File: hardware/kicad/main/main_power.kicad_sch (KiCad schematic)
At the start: 20 parts, among them J1 LINK, U1 RT9080-33GJ5, U2 TPS22917DBVR

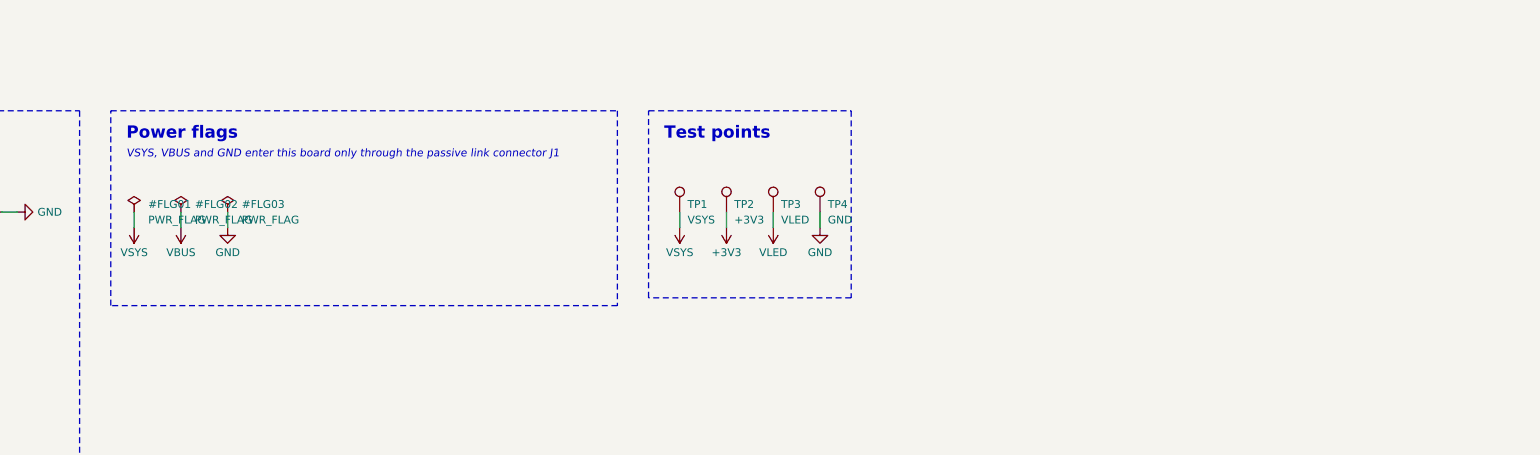
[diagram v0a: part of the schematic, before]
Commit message: Plated GND spindle holes as ESD bleed for the flywheel ring; LED B-variant caveat
Co-Authored-By: Claude Opus 5.5 <noreply@anthropic.com>
Claude-Session: https://claude.ai/code/session_01P3cqdBhxLcWY3sGUVf9LAJ
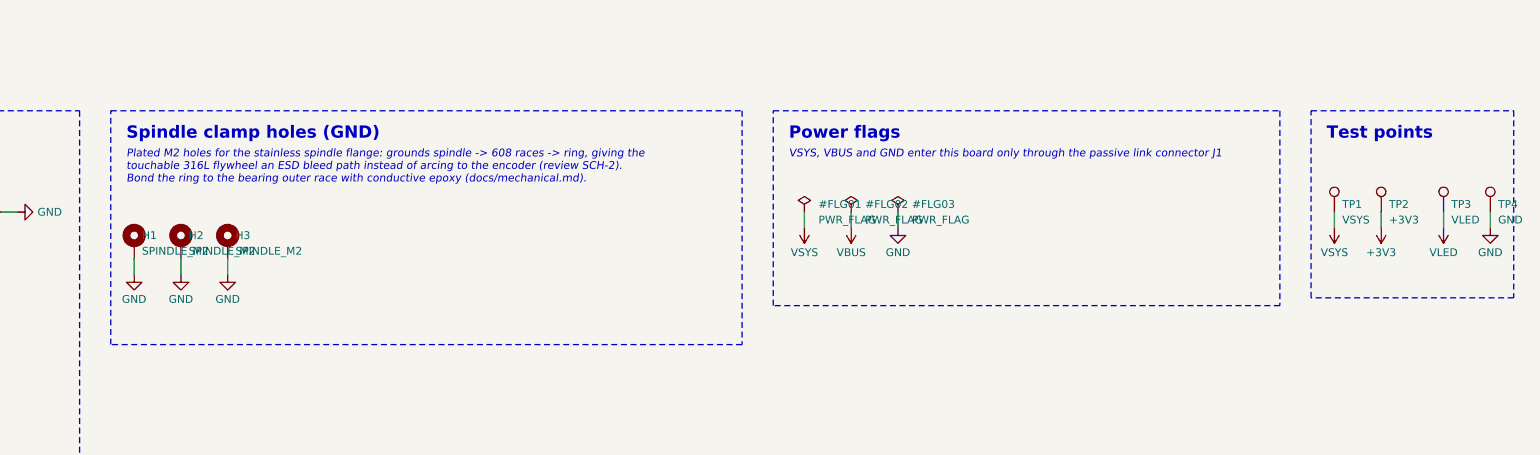
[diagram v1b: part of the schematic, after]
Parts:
- added H1, H2, H3: SPINDLE_M2, MountingHole:MountingHole_2.2mm_M2_Pad_Via, symbol Mechanical:MountingHole_Pad
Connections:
- net GND: now also H1.1, H2.1, H3.1
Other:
- note added: "Plated M2 holes for the stainless spindle flange: grounds spindle -> 608 races -> ring, giving the touchable 316L flywheel an ESD bleed path instead of arcing to the encoder (review SCH-2). Bond the ring to the bearing outer race with conductive epoxy (docs/mechanical.md)."
- note added: "Spindle clamp holes (GND)"
- moved on the sheet: TP1, TP2, TP3, TP4

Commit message: WIP: re-placed boards with fiducials (routing in progress), --finish clean-up step
Co-Authored-By: Claude Opus 5.5 <noreply@anthropic.com>
Claude-Session: https://claude.ai/code/session_01P3cqdBhxLcWY3sGUVf9LAJ
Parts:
- C1, C2, C3, C4, C5, C6, C8, C9: Manufacturer (none) -> Samsung Electro-Mechanics
- C7: Manufacturer (none) -> FH
- R1, R2, R3, R4: Manufacturer (none) -> UNI-ROYAL
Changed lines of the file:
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@@
 			)
 		)
+		(property "Manufacturer" "Samsung Electro-Mechanics"
+			(at 55.88 38.1 0)
+			(effects
+				(font
+					(size 1.27 1.27)
+				)
+				(hide yes)
+			)
+		)
 		(property "LCSC" "C45783"
 			(at 55.88 38.1 0)
@@
 			)
 		)
+		(property "Manufacturer" "Samsung Electro-Mechanics"
+			(at 193.04 35.56 0)
+			(effects
+				(font
+					(size 1.27 1.27)
+				)
+				(hide yes)
+			)
+		)
 		(property "LCSC" "C19702"
 			(at 193.04 35.56 0)
@@
 			)
 		)
+		(property "Manufacturer" "Samsung Electro-Mechanics"
+			(at 223.52 35.56 0)
+			(effects
+				(font
+					(size 1.27 1.27)
+				)
+				(hide yes)
+			)
+		)
 		(property "LCSC" "C19702"
 			(at 223.52 35.56 0)
@@
 			)
 		)
+		(property "Manufacturer" "Samsung Electro-Mechanics"
+			(at 256.54 35.56 0)
+			(effects
+				(font
+					(size 1.27 1.27)
+				)
+				(hide yes)
+			)
+		)
 		(property "LCSC" "C1525"
 			(at 256.54 35.56 0)
@@
 			)
 		)
+		(property "Manufacturer" "UNI-ROYAL"
+			(at 292.1 35.56 0)
+			(effects
+				(font
+					(size 1.27 1.27)
+				)
+				(hide yes)
+			)
+		)
 		(property "LCSC" "C11490"
 			(at 292.1 35.56 0)
@@
 			)
 		)
+		(property "Manufacturer" "UNI-ROYAL"
+			(at 337.82 35.56 0)
+			(effects
+				(font
+					(size 1.27 1.27)
+				)
+				(hide yes)
+			)
+		)
 		(property "LCSC" "C26083"
 			(at 337.82 35.56 0)
@@
 			)
 		)
+		(property "Manufacturer" "Samsung Electro-Mechanics"
+			(at 375.92 35.56 0)
+			(effects
+				(font
+					(size 1.27 1.27)
+				)
+				(hide yes)
+			)
+		)
 		(property "LCSC" "C1525"
 			(at 375.92 35.56 0)
@@
 			)
 		)
+		(property "Manufacturer" "Samsung Electro-Mechanics"
+			(at 83.82 111.76 0)
+			(effects
+				(font
+					(size 1.27 1.27)
+				)
+				(hide yes)
+			)
+		)
 		(property "LCSC" "C19702"
 			(at 83.82 111.76 0)
@@
 			)
 		)
+		(property "Manufacturer" "FH"
+			(at 116.84 111.76 0)
+			(effects
+				(font
+					(size 1.27 1.27)
+				)
+				(hide yes)
+			)
+		)
 		(property "LCSC" "C1523"
 			(at 116.84 111.76 0)
@@
 			)
 		)
+		(property "Manufacturer" "UNI-ROYAL"
+			(at 154.94 111.76 0)
+			(effects
+				(font
+					(size 1.27 1.27)
+				)
+				(hide yes)
+			)
+		)
 		(property "LCSC" "C25741"
 			(at 154.94 111.76 0)
@@
 			)
 		)
+		(property "Manufacturer" "UNI-ROYAL"
+			(at 27.94 149.86 0)
+			(effects
+				(font
+					(size 1.27 1.27)
+				)
+				(hide yes)
+			)
+		)
 		(property "LCSC" "C25076"
 			(at 27.94 149.86 0)
@@
 			)
 		)
+		(property "Manufacturer" "Samsung Electro-Mechanics"
+			(at 63.5 149.86 0)
+			(effects
+				(font
+					(size 1.27 1.27)
+				)
+				(hide yes)
+			)
+		)
 		(property "LCSC" "C45783"
 			(at 63.5 149.86 0)
@@
 			(at 96.52 149.86 0)
 			(effects
+				(font
+					(size 1.27 1.27)
+				)
+				(hide yes)
+			)
+		)
+		(property "Manufacturer" "Samsung Electro-Mechanics"
+			(at 96.52 149.86 0)
+			(effects

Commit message: Main schematic: ERC clean (VBUS_NRF power flag, documented waiver for U21 QOD tied to VOUT); Freerouting pass cap; load-switch test numerics fallback
- build.py: ERC_WAIVERS lists intended pin-type violations; waived ones are reported as such, never dropped
- mcu.py: PWR_FLAG on VBUS_NRF (fed from VBUS through R12)
- display.py: L20 note gives Isat 0.72 A rated (0.92 A typical)
- layout.py: also pass --router.max_passes (Freerouting 2.1 ignores -mp)
- test_load_switches.py: run() retries stalled/hung decks with looser numerics (verifier NEW-6)

Co-Authored-By: Claude Opus 5.5 <noreply@anthropic.com>
Claude-Session: https://claude.ai/code/session_01P3cqdBhxLcWY3sGUVf9LAJ
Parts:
- C2, C6: value 10u -> 10u/25V; LCSC C19702 -> C96446; MPN CL10A106KP8NNNC -> CL10A106MA8NRNC
- R4: value 100 -> 68; LCSC C25076 -> C163455; MPN 0402WGF1000TCE -> RC0402FR-0768RL; Manufacturer UNI-ROYAL -> YAGEO
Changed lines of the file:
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@@
 			)
 		)
-		(property "Value" "10u"
+		(property "Value" "10u/25V"
 			(at 193.04 39.192 90)
 			(effects
@@
 			)
 		)
-		(property "MPN" "CL10A106KP8NNNC"
+		(property "MPN" "CL10A106MA8NRNC"
 			(at 193.04 35.56 0)
 			(effects
@@
 			)
 		)
-		(property "LCSC" "C19702"
+		(property "LCSC" "C96446"
 			(at 193.04 35.56 0)
 			(effects
@@
 			)
 		)
-		(property "Value" "10u"
+		(property "Value" "10u/25V"
 			(at 83.82 115.392 90)
 			(effects
@@
 			)
 		)
-		(property "MPN" "CL10A106KP8NNNC"
+		(property "MPN" "CL10A106MA8NRNC"
 			(at 83.82 111.76 0)
 			(effects
@@
 			)
 		)
-		(property "LCSC" "C19702"
+		(property "LCSC" "C96446"
 			(at 83.82 111.76 0)
 			(effects
@@
 			)
 		)
-		(property "Value" "100"
+		(property "Value" "68"
 			(at 27.94 152.476 90)
 			(effects
@@
 			)
 		)
-		(property "Description" "QOD discharge resistor (TPS22917 option 1: external R between VOUT and QOD); ~4 ms with 44 uF"
+		(property "Description" "QOD discharge resistor (TPS22917 option 1: external R between VOUT and QOD); VLED to 10 % in <= 28.3 ms at the C8/C9 +20 % corner, inside the firmware's 30 ms (hardware/sim test_load_switches)"
 			(at 27.94 149.86 0)
 			(effects
@@
 			)
 		)
-		(property "MPN" "0402WGF1000TCE"
+		(property "MPN" "RC0402FR-0768RL"
 			(at 27.94 149.86 0)
 			(effects
@@
 			)
 		)
-		(property "Manufacturer" "UNI-ROYAL"
+		(property "Manufacturer" "YAGEO"
 			(at 27.94 149.86 0)
 			(effects
@@
 			)
 		)
-		(property "LCSC" "C25076"
+		(property "LCSC" "C163455"
 			(at 27.94 149.86 0)
 			(effects

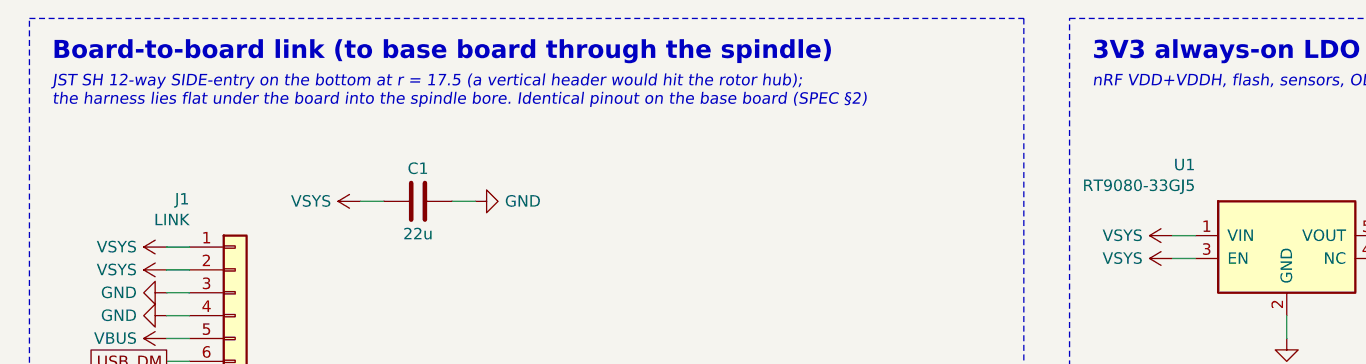
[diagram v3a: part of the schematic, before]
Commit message: Schematic notes: J1 at r 19.5, VLED fall 24/26.6 ms, hot-plug 4.49-5.49 V, SM04B J2, 100k press pull-down, SYS_REG 4.4 V, side-entry J3, LED data path and margins
Notes only; netlists unchanged. Base board still DRC-clean with schematic parity.

Co-Authored-By: Claude Opus 5.5 <noreply@anthropic.com>
Claude-Session: https://claude.ai/code/session_01P3cqdBhxLcWY3sGUVf9LAJ
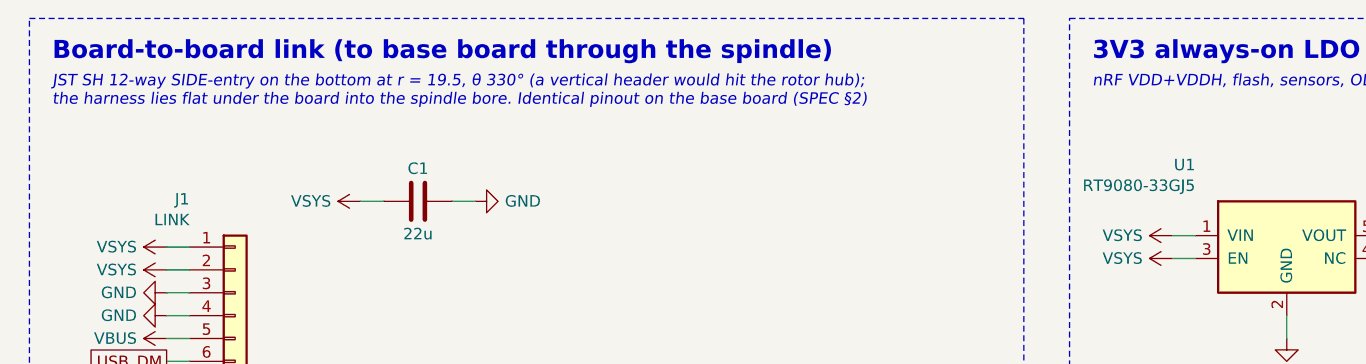
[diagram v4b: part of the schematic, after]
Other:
- note added: "JST SH 12-way SIDE-entry on the bottom at r = 19.5, θ 330° (a vertical header would hit the rotor hub); the harness lies flat under the board into the spindle bore. Identical pinout on the base board (SPEC §2)"
- note removed: "JST SH 12-way SIDE-entry on the bottom at r = 17.5 (a vertical header would hit the rotor hub); the harness lies flat under the board into the spindle bore. Identical pinout on the base board (SPEC §2)"
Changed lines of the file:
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@@
 		)
 	)
-	(text "JST SH 12-way SIDE-entry on the bottom at r = 17.5 (a vertical header would hit the rotor hub);\nthe harness lies flat under the board into the spindle bore. Identical pinout on the base board (SPEC §2)"
+	(text "JST SH 12-way SIDE-entry on the bottom at r = 19.5, θ 330° (a vertical header would hit the rotor hub);\nthe harness lies flat under the board into the spindle bore. Identical pinout on the base board (SPEC §2)"
 		(exclude_from_sim no)
 		(at 15.24 24.13 0)
@@
 			)
 		)
-		(property "Description" "QOD discharge resistor (TPS22917 option 1: external R between VOUT and QOD); VLED to 10 % in <= 28.3 ms at the C8/C9 +20 % corner, inside the firmware's 30 ms (hardware/sim test_load_switches)"
+		(property "Description" "QOD discharge resistor (TPS22917 option 1: external R between VOUT and QOD); VLED to 10 % in about 24 ms (26.6 ms worst corner, C8/C9 +20 %, DC bias), inside the firmware's 30 ms (hardware/sim test_u2_qod_discharge_tolerance_extremes)"
 			(at 27.94 149.86 0)
 			(effects
